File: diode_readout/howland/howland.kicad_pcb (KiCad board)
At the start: 4 copper layers, 39 x 23 mm, 36 parts, among them J1 Conn_01x04, J2 JST_SH_Conn_01x04_i2c_horizon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, J5 MMCX-KE-STM, J6 MMCX-KE-STM, U1 MCP3421A0T-ECH, U3 TLV2782IDGKR, U4 REF3225AMDBVREP, U5 INA333xxDGK, U6 AD8628

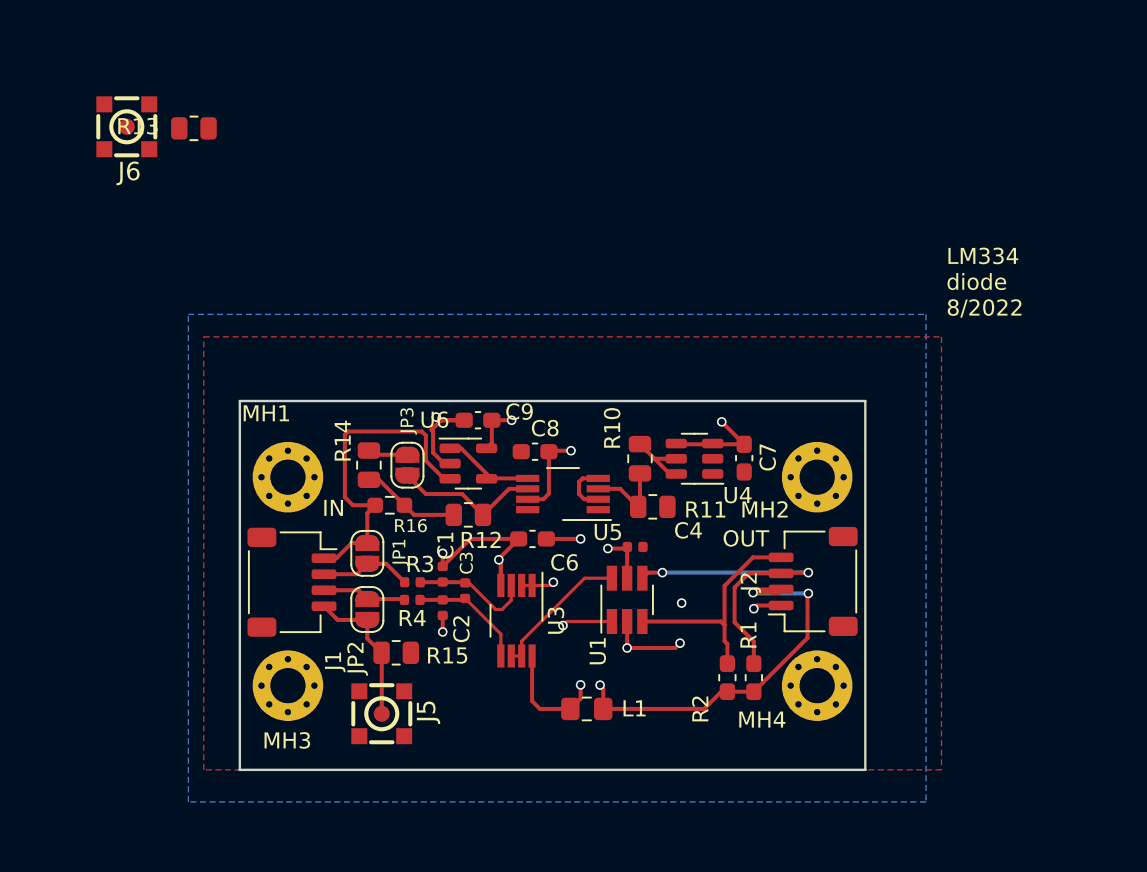
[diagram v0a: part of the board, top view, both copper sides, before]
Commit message: add sq_lockin_v8 and tweaks to howland diode_readout
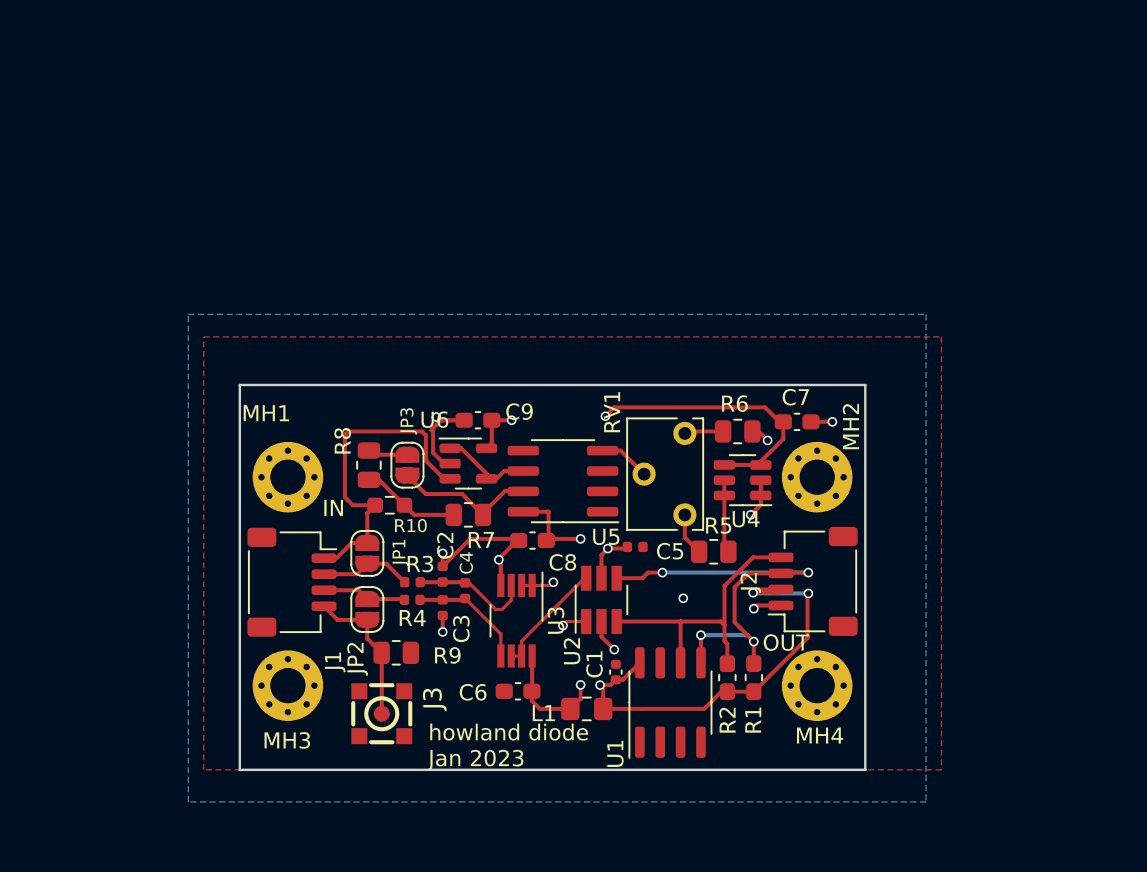
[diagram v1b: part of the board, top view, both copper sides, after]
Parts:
- removed J6: MMCX-KE-STM, 0my_footprints6:MMCX-SMD_KH-MMCX-KE-STM
- removed R13: DNF, Resistor_SMD:R_0805_2012Metric
- added C1: 100nF, Capacitor_SMD:C_0402_1005Metric, F.Cu at (123.5, 96.2)
- added RV1: R_Potentiometer_Trim, Potentiometer_THT:Potentiometer_Bourns_3266W_Vertical, F.Cu at (127.8, 86.3)
- added U1: FM24C64C, Package_SO:SOIC-8_3.9x4.9mm_P1.27mm, F.Cu at (126.8, 98.0)
- R5: renamed from R10; value 1K -> 10K
- R6: renamed from R11; value 1K -> 10K
- U5: value INA333xxDGK -> INA826; footprint Package_SO:VSSOP-8_3.0x3.0mm_P0.65mm -> Package_SO:SOIC-8_3.9x4.9mm_P1.27mm
- moved C6 9.54 mm to (117.3, 97.3)
- moved R5 7.40 mm to (129.6, 88.7), turned to 180 degrees
- moved R6 7.08 mm to (131.1, 81.2)
- moved C8 5.54 mm to (118.2, 88.0)
- moved C7 4.00 mm to (134.8, 80.5), turned to 180 degrees
- moved U4 3.28 mm to (131.3, 84.2)
- moved U2 1.60 mm to (122.5, 91.7)
- moved U5 0.80 mm to (120.2, 84.2)
- renumbered C1 to C2, C2 to C3, C3 to C4, C4 to C5, J5 to J3, R16 to R10, R12 to R7, R14 to R8, R15 to R9, U1 to U2
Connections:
- R5 pad 2: Net-(R10-Pad2) -> Net-(R5-Pad2)
- R6 pad 1: Net-(R10-Pad2) -> Net-(R6-Pad1)
- U5 pad 1: unconnected-(U5-Pad1) -> GND
- U5 pad 2: GND -> unconnected-(U5-Pad2)
- U5 pad 3: Net-(R10-Pad2) -> unconnected-(U5-Pad3)
- U5 pad 4: GND -> Net-(RV1-Pad2)
- U5 pad 5: Net-(U5-Pad5) -> GND
- U5 pad 6: Net-(JP3-Pad1) -> Net-(U5-Pad6)
- U5 pad 7: +3V3 -> Net-(JP3-Pad1)
- U5 pad 8: unconnected-(U5-Pad8) -> +3V3
- U6 pad 1: Net-(U5-Pad5) -> Net-(U5-Pad6)
- U6 pad 4: Net-(U5-Pad5) -> Net-(U5-Pad6)
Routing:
- net /sda-tx: track 20.7 -> 27.4 mm, vias 2 -> 4
- net Net-(U5-Pad5): track 5.78 -> 0.00 mm
- net Net-(U5-Pad6): track 0.00 -> 5.73 mm
- net Net-(R10-Pad2): track 4.93 -> 0.00 mm
- net /scl-rx: track 14.4 -> 18.6 mm
- net Net-(RV1-Pad2): track 0.00 -> 3.19 mm
- net VD: track 37.7 -> 40.8 mm
- net Net-(R5-Pad2): track 0.00 -> 2.67 mm
- net Net-(R6-Pad1): track 0.00 -> 2.27 mm
- net +3V3: track 53.5 -> 55.2 mm, vias 5 -> 4
- net /Channel1/buffer/out-: track 8.83 -> 7.23 mm
- net /Channel1/buffer/out+: track 8.16 -> 6.56 mm
- net GND: track 31.7 -> 32.9 mm, vias 8 -> 10
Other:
- board size 39 x 23 mm -> 39 x 24 mm
- board text added: "howland diode Jan 2023"
- board text removed: "LM334 diode 8/2022"

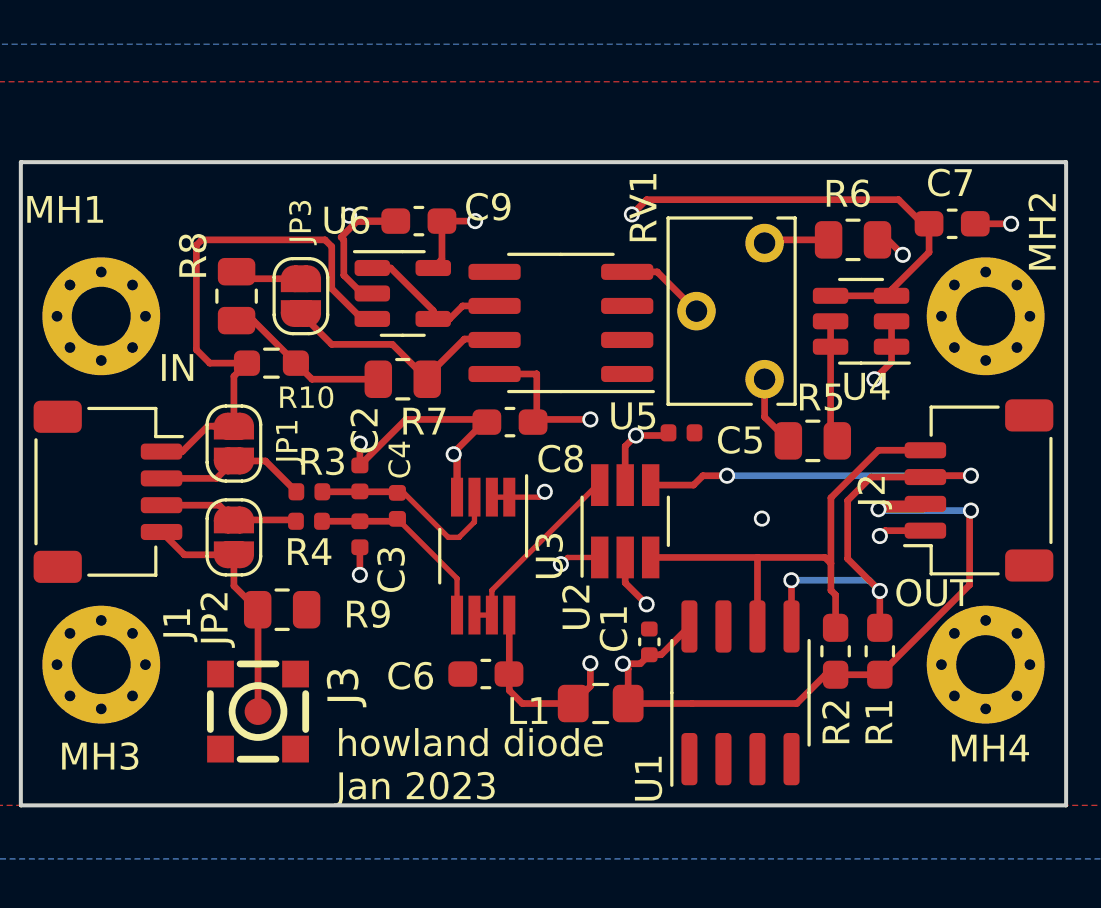
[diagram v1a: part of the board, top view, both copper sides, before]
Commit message: Commit changes to howland current source diode readout: 1.  Add 1Mohm shorts bettern V+ and I+  as well as V- and I- to mimic      this will mimic the two wire readout behaviour when the diode gets      disconnected. 2.  Add FRAM chip, 512kbits or 64kBytes of memory
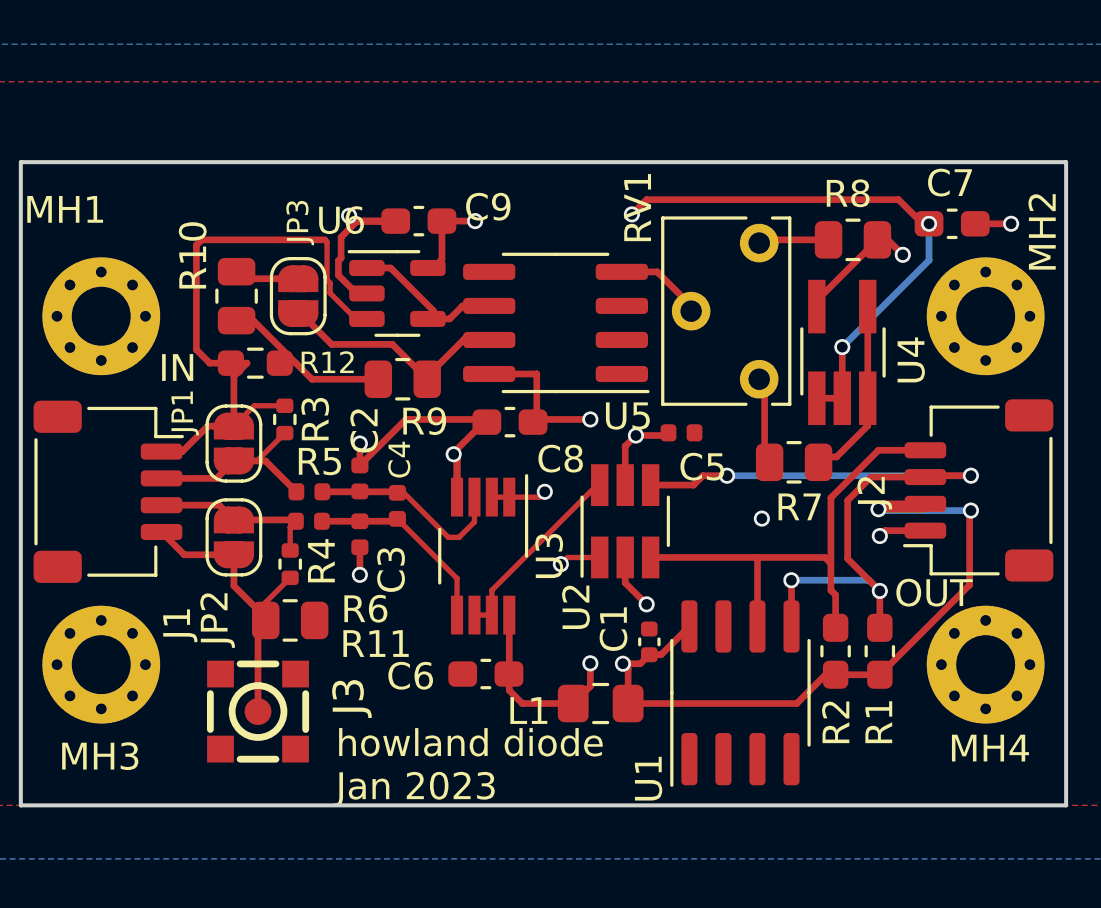
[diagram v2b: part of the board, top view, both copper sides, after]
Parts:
- added R3: 1M, Resistor_SMD:R_0402_1005Metric, F.Cu at (109.8, 87.8)
- added R4: 1M, Resistor_SMD:R_0402_1005Metric, F.Cu at (110.0, 93.2)
- U4: value REF3225AMDBVREP -> ADR391; footprint Package_TO_SOT_SMD:SOT-23-6 -> Package_TO_SOT_SMD:TSOT-23-5_HandSoldering
- moved U4 1.36 mm to (130.7, 85.3), turned to 90 degrees
- moved R7 1.06 mm to (128.8, 89.5)
- moved R12 0.60 mm to (108.8, 85.8)
- moved R11 0.50 mm to (110.0, 95.3)
- moved RV1 0.20 mm to (127.5, 86.3)
- moved U5 0.20 mm to (120.0, 84.2)
- moved U6 0.20 mm to (114.0, 83.2)
- moved JP3 0.10 mm to (110.3, 83.2)
- renumbered R8 to R10, R9 to R11, R10 to R12, R3 to R5, R4 to R6, R5 to R7, R6 to R8, R7 to R9
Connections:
- R7 pad 1: Net-(R5-Pad1) -> Net-(R7-Pad1)
- U4 pad 1: GND -> +3V3
- U4 pad 2: GND -> +3V3
- U4 pad 3: +3V3 -> Net-(R7-Pad1)
- U4 pad 4: +3V3 -> Net-(R7-Pad1)
- U4 pad 5: Net-(R5-Pad1) -> GND
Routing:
- net Net-(R7-Pad1): track 0.00 -> 6.76 mm
- net Net-(R5-Pad1): track 4.21 -> 0.00 mm
- net +3V3: track 55.2 -> 58.5 mm, vias 4 -> 6
- net /Channel1/I+: track 20.0 -> 22.6 mm
- net /Channel1/V+: track 5.78 -> 8.11 mm
- net /Channel1/I-: track 9.26 -> 11.2 mm
- net /Channel1/V-: track 5.19 -> 6.37 mm
- net GND: track 32.9 -> 34.1 mm, vias 10 -> 9
- net Net-(JP3-Pad1): track 8.94 -> 8.40 mm

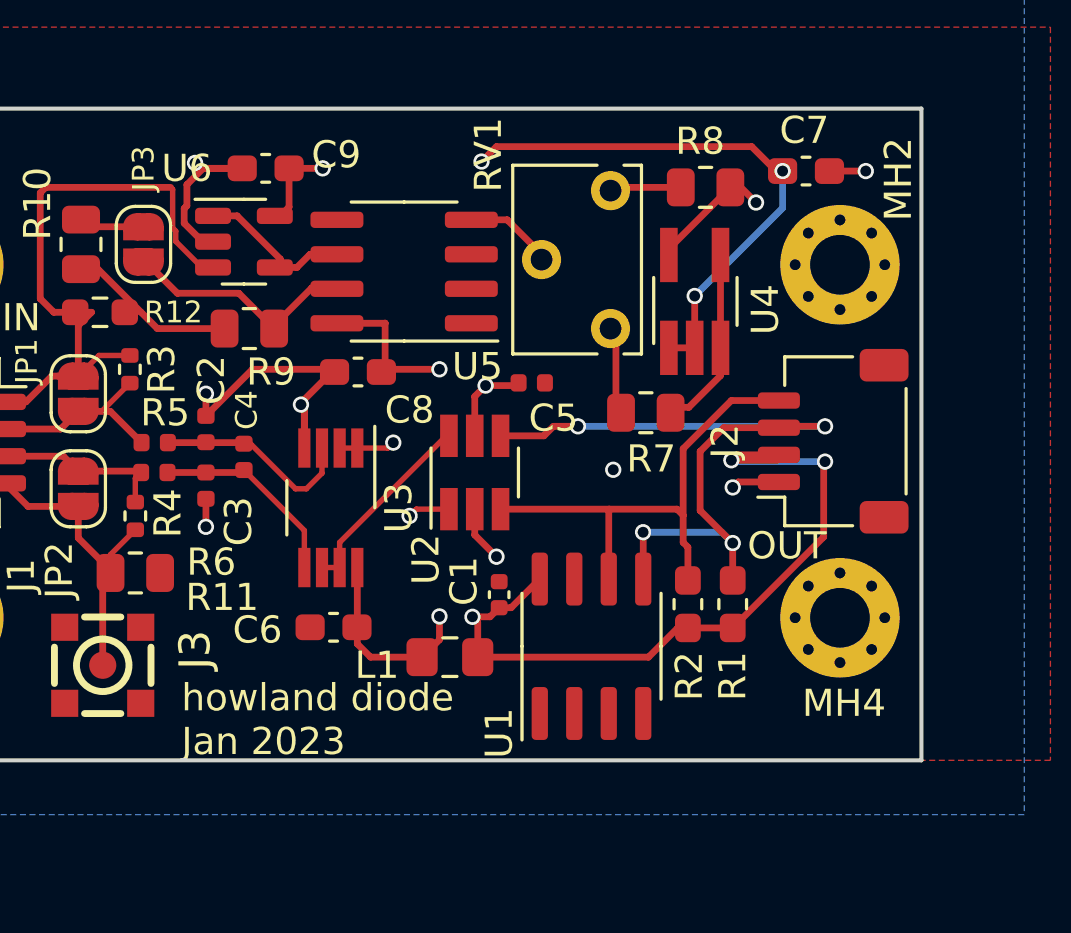
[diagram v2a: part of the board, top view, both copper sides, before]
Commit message: Add tweaks to diode readout
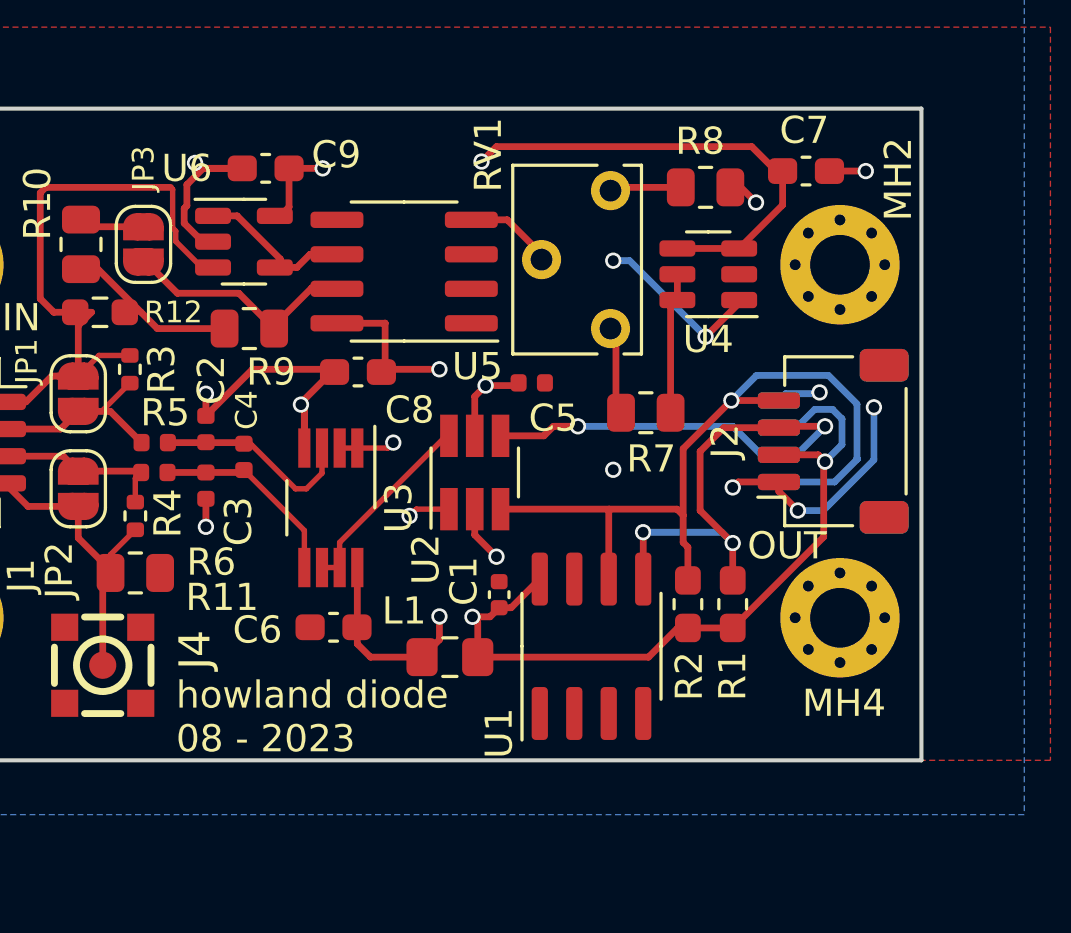
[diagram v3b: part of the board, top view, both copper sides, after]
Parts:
- added J3: JST_SH_Conn_01x04_i2c_horizontal, Connector_JST:JST_SH_SM04B-SRSS-TB_1x04-1MP_P1.00mm_Horizontal, B.Cu at (135.8, 90.5)
- U1: value FM24C64C -> FM24V05
- U4: value ADR391 -> REF3425IDBVR; footprint Package_TO_SOT_SMD:TSOT-23-5_HandSoldering -> Package_TO_SOT_SMD:SOT-23-6
- moved U4 1.12 mm to (131.2, 84.3), turned to 180 degrees
- renumbered J3 to J4
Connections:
- U4 pad 1: +3V3 -> GND
- U4 pad 2: +3V3 -> GND
- U4 pad 3: Net-(R7-Pad1) -> +3V3
- U4 pad 4: Net-(R7-Pad1) -> +3V3
- U4 pad 5: GND -> Net-(R7-Pad1)
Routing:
- net GND: track 34.1 -> 45.3 mm, vias 9 -> 14
- net /scl-rx: track 18.6 -> 29.3 mm, vias 0 -> 1
- net +3V3: track 58.5 -> 55.5 mm, vias 6 -> 4
- net Net-(R7-Pad1): track 6.76 -> 5.20 mm
- net VD: track 40.8 -> 39.6 mm, vias 4 -> 3
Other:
- board text added: "howland diode 08 - 2023"
- board text removed: "howland diode Jan 2023"
